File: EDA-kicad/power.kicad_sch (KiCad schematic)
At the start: 86 parts, among them SW1 EG25-switch-CSS-1210MC, SW2 MIC-switch-CSS-1210MC, SW3 CAM-switch-CSS-1210MC, U11 TPS65023BRSBR, U4 BQ25792RQMR, U6 BAT-CONNECTOR-FLTS22WR00, U7 22V-boost-AP3032KTR-G1, U8 MP3429GL-Z

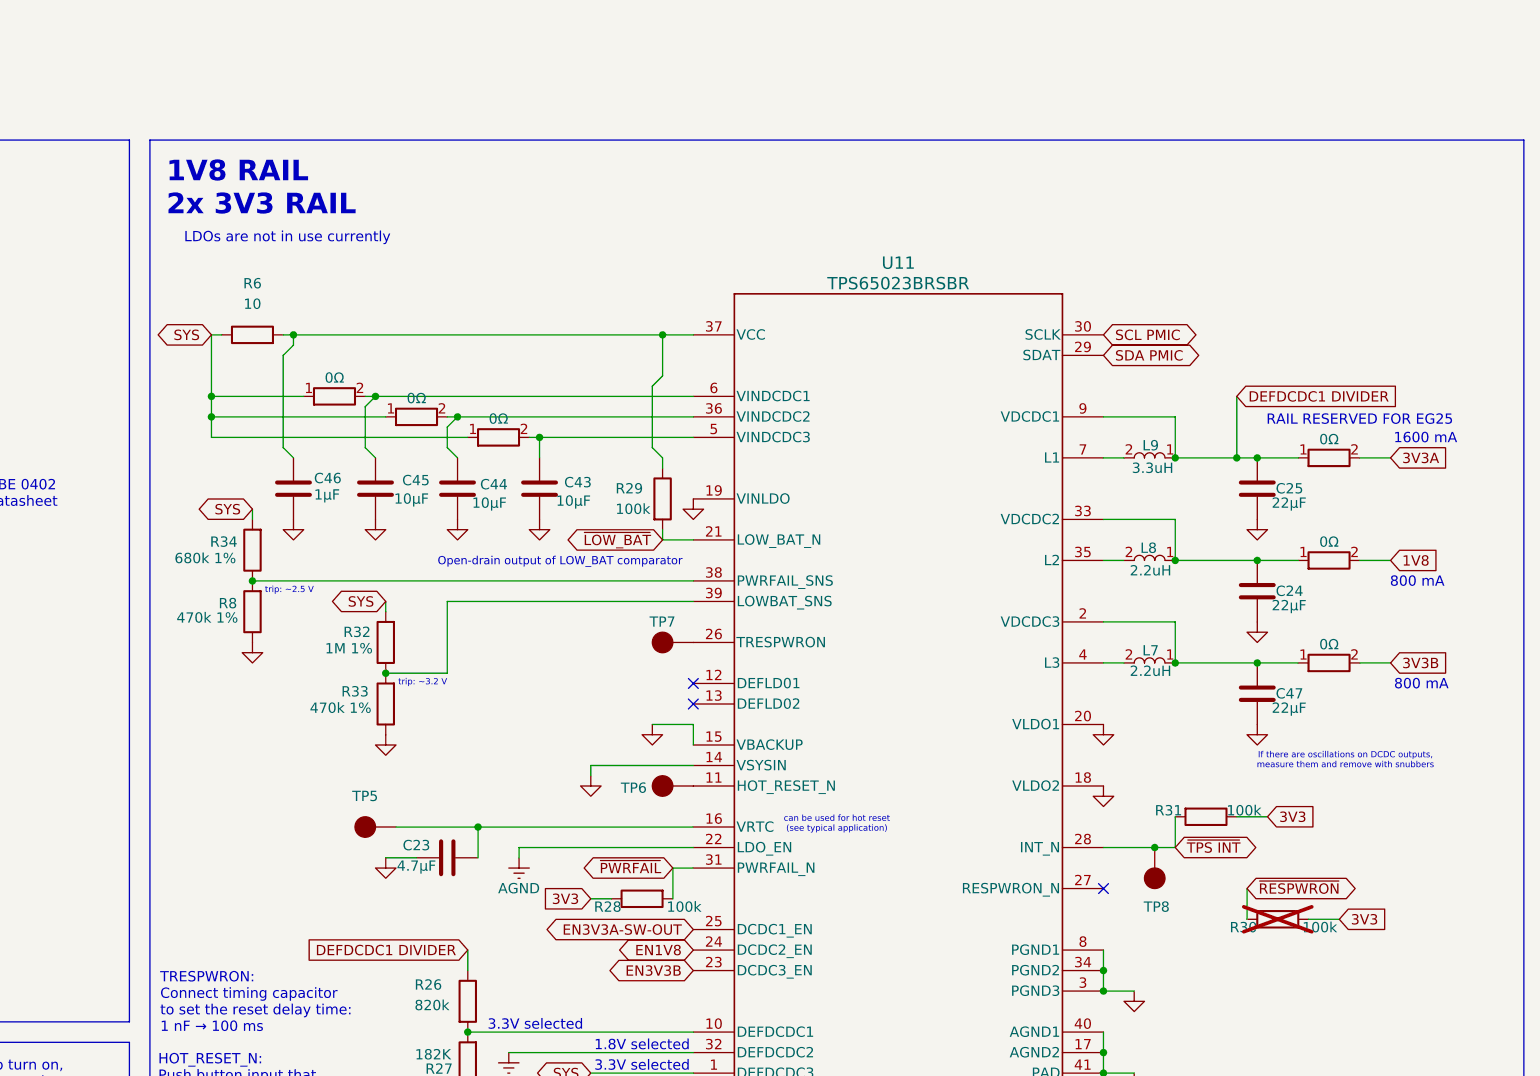
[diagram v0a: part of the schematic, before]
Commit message: fix bad label 3V3
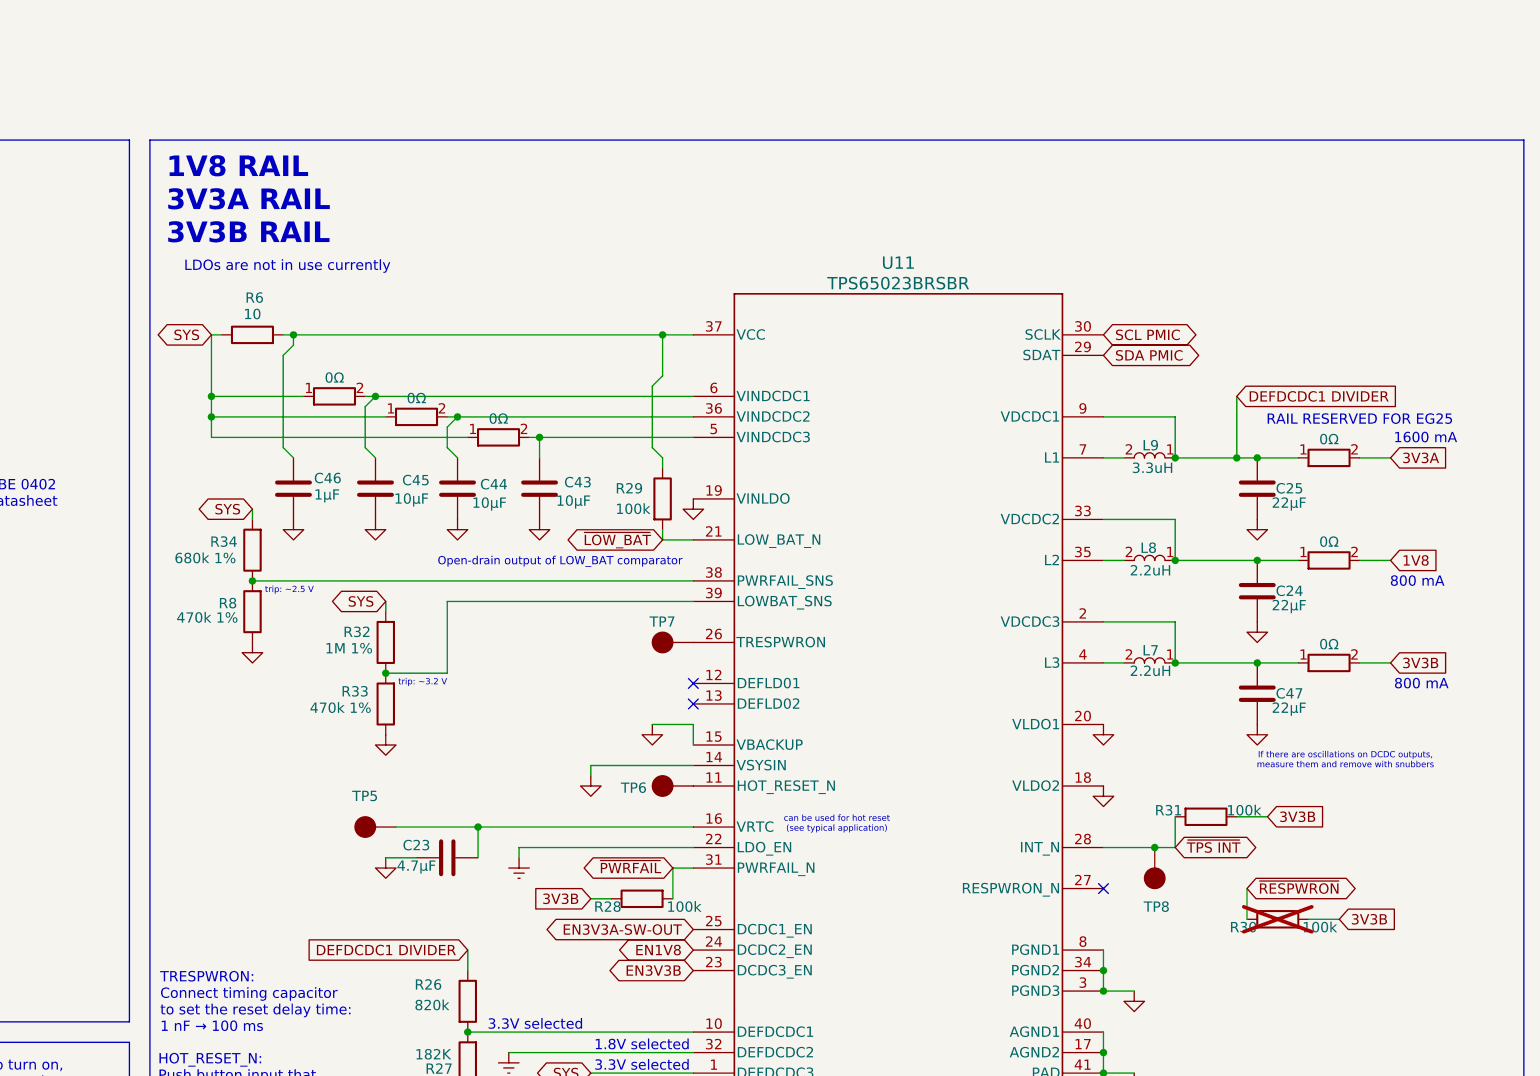
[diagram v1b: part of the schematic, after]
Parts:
- added C24, C25: 22μF, SPIRIT-footprints:0603-capacitor, symbol Device:C
- added R10, R11, R12, R35, R36: 0Ω, SPIRIT-footprints:1K-05W-0805-RES_ERJP06J102V, symbol SPIRIT-components:1K-05W-0805-RES_ERJP06J102V
- renumbered C25 to C47, R11 to R37
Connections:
- net 3V3 is gone; now on net 3V3B: R28.1, R30.2, R31.1
- net 1V8: now also R10.2; no longer R37.2
- net 3V3A: now also R11.2; no longer R37.2
- net DEFDCDC1 DIVIDER: now also C25.1, R11.1; no longer C47.1, R37.1
- net GND: now also C24.2, C25.2
- net SYS: now also R12.1, R35.1, R36.1; no longer R37.1
- net at L8.1, U11.33 (VDCDC2): now also C24.1, R10.1; no longer C47.1, R37.1
- net at C45.1, U11.6 (VINDCDC1): now also R12.2; no longer R37.2
- net at C43.1, U11.5 (VINDCDC3): now also R36.2; no longer R37.2
- net at C44.1, U11.36 (VINDCDC2): now also R35.2; no longer R37.2
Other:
- note added: "1V8 RAIL 3V3A RAIL 3V3B RAIL"
- note removed: "1V8 RAIL 2x 3V3 RAIL"
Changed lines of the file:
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@@
 		)
 	)
-	(text "1V8 RAIL\n2x 3V3 RAIL"
+	(text "1V8 RAIL\n3V3A RAIL\n3V3B RAIL"
 		(exclude_from_sim no)
-		(at 238.252 56.896 0)
+		(at 238.252 58.42 0)
 		(effects
 			(font
@@
 	(text "LDOs are not in use currently"
 		(exclude_from_sim no)
-		(at 253.238 62.992 0)
+		(at 253.238 66.548 0)
 		(effects
 			(font
@@
 		)
 	)
+	(global_label "3V3B"
+		(shape input)
+		(at 290.83 144.78 180)
+		(fields_autoplaced yes)
+		(effects
+			(font
+				(size 1.27 1.27)
+			)
+			(justify right)
+		)
+		(property "Intersheetrefs" "${INTERSHEET_REFS}"
+			(at 283.0672 144.78 0)
+			(effects
+				(font
+					(size 1.27 1.27)
+				)
+				(justify right)
+				(hide yes)
+			)
+		)
+	)
 	(global_label "REGN"
 		(shape bidirectional)
@@
 		)
 	)
+	(global_label "3V3B"
+		(shape input)
+		(at 383.54 147.32 0)
+		(fields_autoplaced yes)
+		(effects
+			(font
+				(size 1.27 1.27)
+			)
+			(justify left)
+		)
+		(property "Intersheetrefs" "${INTERSHEET_REFS}"
+			(at 391.3028 147.32 0)
+			(effects
+				(font
+					(size 1.27 1.27)
+				)
+				(justify left)
+				(hide yes)
+			)
+		)
+	)
 	(global_label "REGN"
 		(shape bidirectional)
@@
 		)
 	)
-	(global_label "3V3"
-		(shape input)
-		(at 290.83 144.78 180)
-		(fields_autoplaced yes)
-		(effects
-			(font
-				(size 1.27 1.27)
-			)
-			(justify right)
-		)
-		(property "Intersheetrefs" "${INTERSHEET_REFS}"
-			(at 284.3372 144.78 0)
-			(effects
-				(font
-					(size 1.27 1.27)
-				)
-				(justify right)
-				(hide yes)
-			)
-		)
-	)
 	(global_label "SDA"
 		(shape bidirectional)
@@
 		)
 	)
-	(global_label "3V3"
-		(shape input)
-		(at 374.65 134.62 0)
-		(fields_autoplaced yes)
-		(effects
-			(font
-				(size 1.27 1.27)
-			)
-			(justify left)
-		)
-		(property "Intersheetrefs" "${INTERSHEET_REFS}"
-			(at 381.1428 134.62 0)
-			(effects
-				(font
-					(size 1.27 1.27)
-				)
-				(justify left)
-				(hide yes)
-			)
-		)
-	)
 	(global_label "SYS"
 		(shape bidirectional)
@@
 		)
 	)
+	(global_label "3V3B"
+		(shape input)
+		(at 374.65 134.62 0)
+		(fields_autoplaced yes)
+		(effects
+			(font
+				(size 1.27 1.27)
+			)
+			(justify left)
+		)
+		(property "Intersheetrefs" "${INTERSHEET_REFS}"
+			(at 382.4128 134.62 0)
+			(effects
+				(font
+					(size 1.27 1.27)
+				)
+				(justify left)
+				(hide yes)
+			)
+		)
+	)
 	(global_label "SYS"
 		(shape bidirectional)
@@
 		)
 	)
-	(global_label "3V3"
-		(shape input)
-		(at 383.54 147.32 0)
-		(fields_autoplaced yes)
-		(effects
-			(font
-				(size 1.27 1.27)
-			)
-			(justify left)
-		)
-		(property "Intersheetrefs" "${INTERSHEET_REFS}"
-			(at 390.0328 147.32 0)
-			(effects
-				(font
-					(size 1.27 1.27)
-				)
-				(justify left)
-				(hide yes)
-			)
-		)
-	)
 	(symbol
 		(lib_id "Device:R")
@@
 					(size 1.27 1.27)
 				)
+				(hide yes)
 			)
 		)
@@
 		(on_board yes)
 		(dnp no)
-		(fields_autoplaced yes)
 		(property "Reference" "R6"
-			(at 248.92 68.58 90)
+			(at 249.174 70.358 90)
 			(effects
 				(font
@@
 		)
 		(property "Value" "10"
-			(at 248.92 71.12 90)
+			(at 248.92 72.39 90)
 			(effects
 				(font

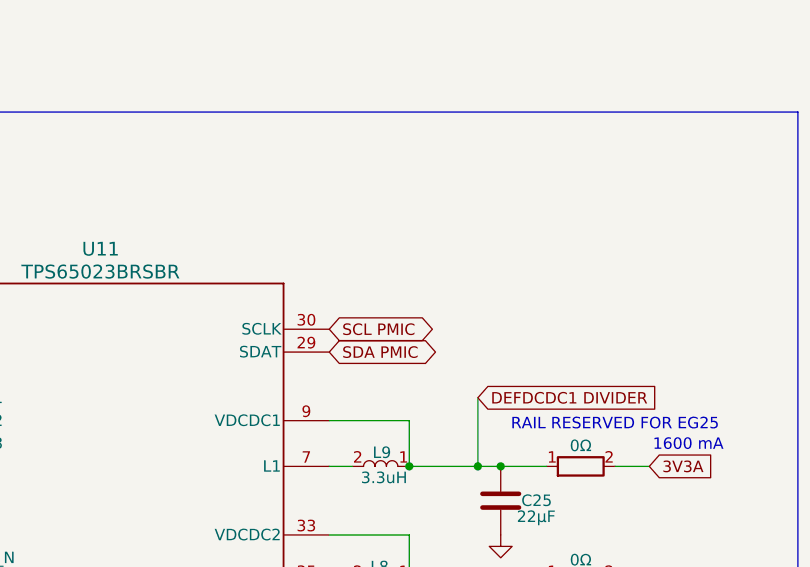
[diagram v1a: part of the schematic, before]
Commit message: pull up I2C line of TPS
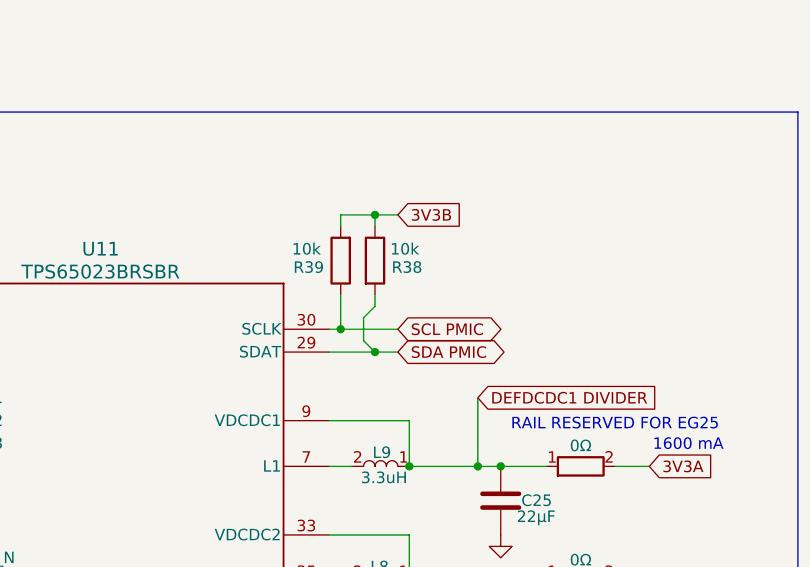
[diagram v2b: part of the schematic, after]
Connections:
- net 3V3B: now also R18.1, R18.2
- net SCL PMIC: now also R18.1
- net SDA PMIC: now also R18.2
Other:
- moved on the sheet: R38
